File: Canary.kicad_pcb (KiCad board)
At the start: 4 copper layers, 56 x 38 mm, 85 parts, among them J1 CONN_ARM_CM_JTAG_SWD_10, J2 20021311-00010T4LF, J3 USB4125-GF-A, J4 S2B-PH-SM4-TB, Q1 PMN30UNX, Q2 PMN42XPEAH, Q3 PMN30UNX, SW1 TL3301SPF160QJ, U1 BMD-300-A-R, U10 LP5907MFX-3.2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

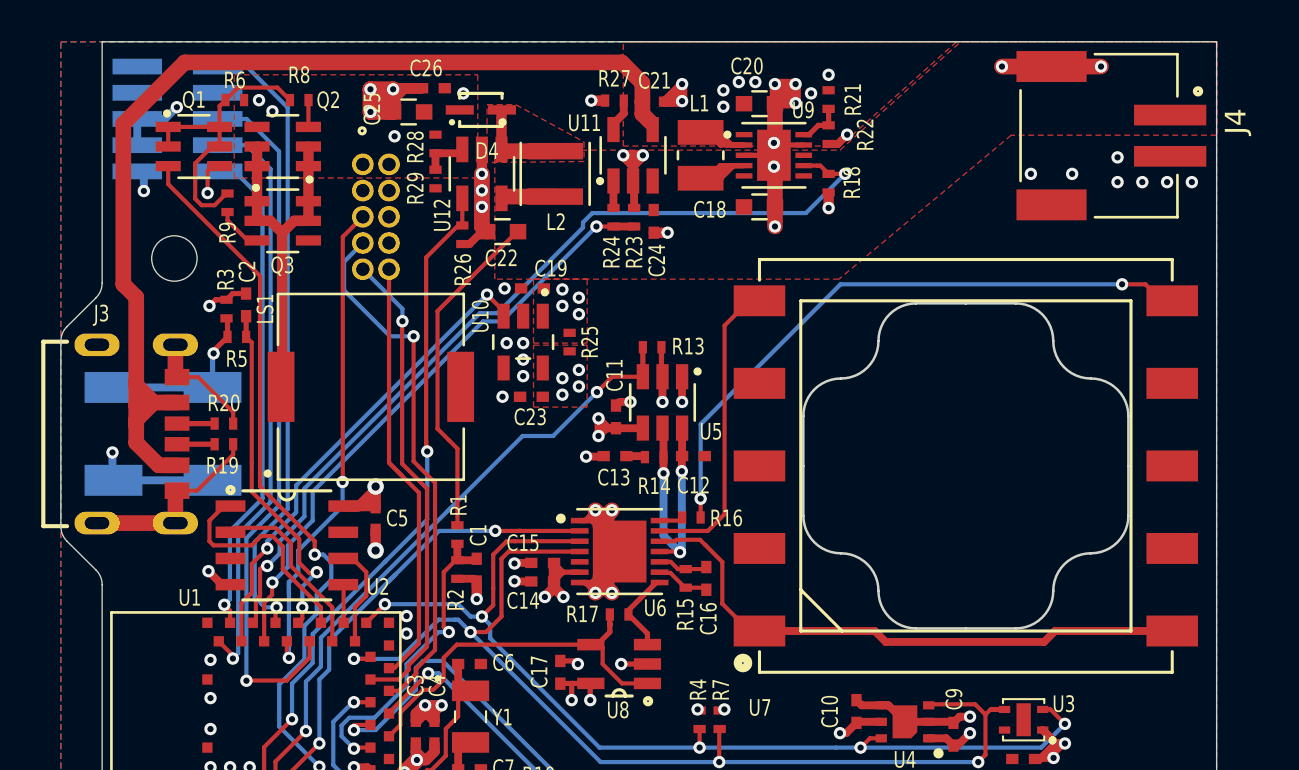
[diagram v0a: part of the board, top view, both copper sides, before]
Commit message: Change crystal
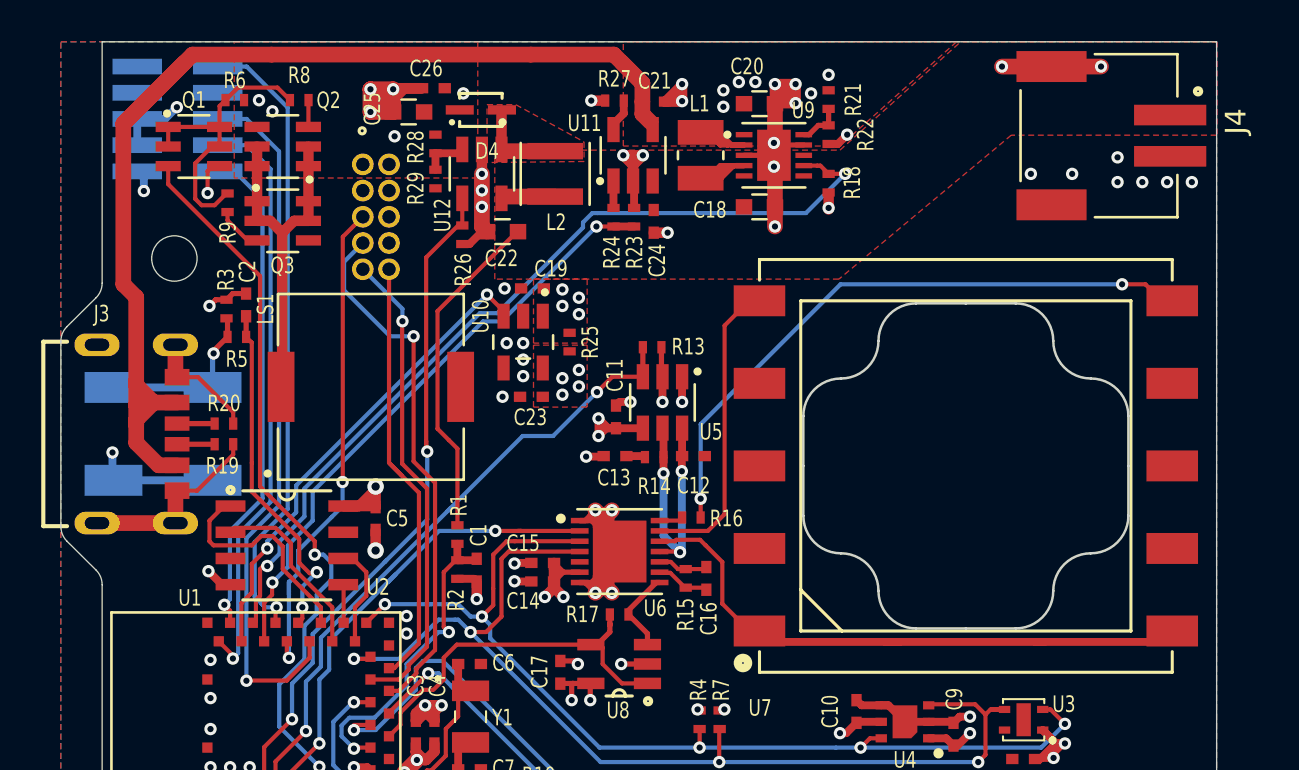
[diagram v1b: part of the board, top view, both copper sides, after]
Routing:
- net VBUS: track 51.8 -> 57.8 mm
- net /Potentiostat/SPEC_WE: track 28.0 -> 29.0 mm
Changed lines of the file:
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@@
     (thickness 1.6)
     (drawings 12)
-    (tracks 942)
+    (tracks 948)
     (zones 0)
     (modules 85)
@@
   )
   (setup
-    (last_trace_width 0.2032)
+    (last_trace_width 0.381)
     (user_trace_width 0.1524)
     (user_trace_width 0.2032)
@@
     (add_net ~RESET~)
   )
+  (module JetkovKiCADLib:SM-UART-04L locked (layer F.Cu)
+    (at 50.26 48.045)
+    (attr virtual)
+    (fp_text reference S1 (at 48.89 36.48) (layer F.SilkS) hide
+      (effects (font (size 0.8 0.6) (thickness 0.15)))
+    )
+    (fp_text value DNP (at 23.1 16.9) (layer F.Fab) hide
+      (effects (font (size 1 1) (thickness 0.15)))
+    )
+    (fp_line (start 7.65 11.47) (end 4.35 11.47) (layer Dwgs.User) (width 0.12))
+    (fp_line (start 4.35 4.53) (end 4.35 11.47) (layer Dwgs.User) (width 0.12))
+    (fp_line (start 9.5 13.5) (end 2.5 13.5) (layer Dwgs.User) (width 0.12))
+    (fp_line (start 7.65 11.47) (end 7.65 4.53) (layer Dwgs.User) (width 0.12))
+    (fp_line (start 9.5 2.5) (end 9.5 13.5) (layer Dwgs.User) (width 0.12))
+    (fp_line (start 2.5 2.5) (end 9.5 2.5) (layer Dwgs.User) (width 0.12))
+    (fp_line (start 4.35 4.53) (end 7.65 4.53) (layer Dwgs.User) (width 0.12))
+    (fp_line (start 2.5 13.5) (end 2.5 2.5) (layer Dwgs.User) (width 0.12))
+    (fp_line (start 0 0) (end 0 37) (layer Dwgs.User) (width 0.12))
+    (fp_line (start 0 37) (end 48 37) (layer Dwgs.User) (width 0.12))
+    (fp_line (start 48 37) (end 48 1) (layer Dwgs.User) (width 0.12))
+    (fp_line (start 48 1) (end 48 0) (layer Dwgs.User) (width 0.12))
+    (fp_line (start 48 0) (end 0 0) (layer Dwgs.User) (width 0.12))
+    (fp_text user 10 (at 8.4 12.5) (layer Dwgs.User)
+      (effects (font (size 0.8 0.8) (thickness 0.15)))
+    )
+    (fp_text user 9 (at 3.5 12.5) (layer Dwgs.User)
+      (effects (font (size 0.8 0.8) (thickness 0.15)))
+    )
+    (fp_text user 2 (at 8.6 3.6) (layer Dwgs.User)
+      (effects (font (size 0.8 0.8) (thickness 0.15)))
+    )
+    (fp_text user 1 (at 3.5 3.6) (layer Dwgs.User)
+      (effects (font (size 0.8 0.8) (thickness 0.15)))
+    )
+    (model :JetkovKiCADLib:SM-UART-04L.step
+      (offset (xyz 24 -18.5 -3))
+      (scale (xyz 1 1 1))
+      (rotate (xyz 180 0 0))
+    )
+  )
   (module JetkovKiCADLib:TL3301EF160QJ locked (layer B.Cu)
     (at 45.95 67)
@@
     )
   )
-  (module JetkovKiCADLib:SM-UART-04L locked (layer F.Cu)
-    (at 50.26 48.045)
-    (attr virtual)
-    (fp_text reference S1 (at 48.89 36.48) (layer F.SilkS) hide
-      (effects (font (size 0.8 0.6) (thickness 0.15)))
-    )
-    (fp_text value DNP (at 23.1 16.9) (layer F.Fab) hide
-      (effects (font (size 1 1) (thickness 0.15)))
-    )
-    (fp_line (start 7.65 11.47) (end 4.35 11.47) (layer Dwgs.User) (width 0.12))
-    (fp_line (start 4.35 4.53) (end 4.35 11.47) (layer Dwgs.User) (width 0.12))
-    (fp_line (start 9.5 13.5) (end 2.5 13.5) (layer Dwgs.User) (width 0.12))
-    (fp_line (start 7.65 11.47) (end 7.65 4.53) (layer Dwgs.User) (width 0.12))
-    (fp_line (start 9.5 2.5) (end 9.5 13.5) (layer Dwgs.User) (width 0.12))
-    (fp_line (start 2.5 2.5) (end 9.5 2.5) (layer Dwgs.User) (width 0.12))
-    (fp_line (start 4.35 4.53) (end 7.65 4.53) (layer Dwgs.User) (width 0.12))
-    (fp_line (start 2.5 13.5) (end 2.5 2.5) (layer Dwgs.User) (width 0.12))
-    (fp_line (start 0 0) (end 0 37) (layer Dwgs.User) (width 0.12))
-    (fp_line (start 0 37) (end 48 37) (layer Dwgs.User) (width 0.12))
-    (fp_line (start 48 37) (end 48 1) (layer Dwgs.User) (width 0.12))
-    (fp_line (start 48 1) (end 48 0) (layer Dwgs.User) (width 0.12))
-    (fp_line (start 48 0) (end 0 0) (layer Dwgs.User) (width 0.12))
-    (fp_text user 10 (at 8.4 12.5) (layer Dwgs.User)
-      (effects (font (size 0.8 0.8) (thickness 0.15)))
-    )
-    (fp_text user 9 (at 3.5 12.5) (layer Dwgs.User)
-      (effects (font (size 0.8 0.8) (thickness 0.15)))
-    )
-    (fp_text user 2 (at 8.6 3.6) (layer Dwgs.User)
-      (effects (font (size 0.8 0.8) (thickness 0.15)))
-    )
-    (fp_text user 1 (at 3.5 3.6) (layer Dwgs.User)
-      (effects (font (size 0.8 0.8) (thickness 0.15)))
-    )
-    (model :JetkovKiCADLib:SM-UART-04L.step
-      (offset (xyz 24 -18.5 -3))
-      (scale (xyz 1 1 1))
-      (rotate (xyz 180 0 0))
-    )
-  )
   (module Mounting_Holes:MountingHole_2.2mm_M2 locked (layer F.Cu)
     (at 46.5 58.5)
@@
   (segment (start 44.025 51.975) (end 44.025 59.75) (width 0.762) (layer F.Cu) (net 9))
   (segment (start 47 49) (end 44.025 51.975) (width 0.762) (layer F.Cu) (net 9))
-  (segment (start 68.175 49) (end 47 49) (width 0.762) (layer F.Cu) (net 9))
   (segment (start 69.175 50) (end 68.175 49) (width 0.762) (layer F.Cu) (net 9))
   (segment (start 69.175 50.9) (end 69.175 50) (width 0.762) (layer F.Cu) (net 9))
+  (segment (start 47.38 48.62) (end 51.21 48.62) (width 0.762) (layer F.Cu) (net 9))
+  (segment (start 44.025 51.975) (end 47.38 48.62) (width 0.762) (layer F.Cu) (net 9))
+  (segment (start 67.795 48.62) (end 69.175 50) (width 0.762) (layer F.Cu) (net 9))
+  (segment (start 63.77 48.62) (end 67.795 48.62) (width 0.762) (layer F.Cu) (net 9))
+  (segment (start 63.77 48.62) (end 51.21 48.62) (width 0.762) (layer F.Cu) (net 9))
   (via (at 50.6 50.83) (size 0.6) (drill 0.3) (layers F.Cu B.Cu) (net 10))
   (via (at 51.25 51.37) (size 0.6) (drill 0.3) (layers F.Cu B.Cu) (net 10))
@@
   (segment (start 70.98 71.2) (end 70.01 71.2) (width 0.2032) (layer F.Cu) (net 53))
   (segment (start 71.1 71.08) (end 70.98 71.2) (width 0.2032) (layer F.Cu) (net 53))
-  (segment (start 94.85 76.55) (end 89.17 76.55) (width 0.381) (layer F.Cu) (net 54))
-  (segment (start 89.17 76.55) (end 88.64 77.08) (width 0.381) (layer F.Cu) (net 54))
-  (segment (start 88.64 77.08) (end 80.97 77.08) (width 0.381) (layer F.Cu) (net 54))
-  (segment (start 80.44 76.55) (end 74.85 76.55) (width 0.381) (layer F.Cu) (net 54))
-  (segment (start 80.97 77.08) (end 80.44 76.55) (width 0.381) (layer F.Cu) (net 54))
   (segment (start 73.05 75.23) (end 74.45 76.63) (width 0.2032) (layer F.Cu) (net 54))
   (segment (start 73.05 73.207202) (end 73.05 75.23) (width 0.2032) (layer F.Cu) (net 54))
@@
   (segment (start 72.237202 72.397202) (end 71.97 72.13) (width 0.2032) (layer F.Cu) (net 54))
   (segment (start 72.24 72.397202) (end 72.237202 72.397202) (width 0.2032) (layer F.Cu) (net 54))
+  (segment (start 75.38 77.08) (end 81.62 77.08) (width 0.381) (layer F.Cu) (net 54))
+  (segment (start 74.85 76.55) (end 75.38 77.08) (width 0.381) (layer F.Cu) (net 54))
+  (segment (start 81.62 77.08) (end 80.97 77.08) (width 0.381) (layer F.Cu) (net 54))
+  (segment (start 94.32 77.08) (end 88.22 77.08) (width 0.381) (layer F.Cu) (net 54))
+  (segment (start 94.85 76.55) (end 94.32 77.08) (width 0.381) (layer F.Cu) (net 54))
+  (segment (start 88.22 77.08) (end 81.62 77.08) (width 0.381) (layer F.Cu) (net 54))
+  (segment (start 88.64 77.08) (end 88.22 77.08) (width 0.381) (layer F.Cu) (net 54))
   (segment (start 73.16 61.75) (end 74.44 60.47) (width 0.2032) (layer F.Cu) (net 55))
   (segment (start 73.16 70.89) (end 73.16 61.75) (width 0.2032) (layer F.Cu) (net 55))
@@
     (polygon
       (pts
-        (xy 61.2 54.6) (xy 49.4 54.6) (xy 49.4 49.6) (xy 61.2 49.6)
+        (xy 61.2 54.6) (xy 49.4 54.6) (xy 49.4 48) (xy 61.2 48)
       )
     )
@@
     (polygon
       (pts
-        (xy 68 62.6) (xy 62.1 62.6) (xy 62.1 86) (xy 41 86.05) (xy 41 48.05)
+        (xy 68 62.6) (xy 62.1 62.6) (xy 62.1 86) (xy 41 86) (xy 41 48)
         (xy 84.4 48.05)
       )
@@
       )
     )
+  )
+  (zone (net 0) (net_name "") (layers F.Cu GND.Cu PWR.Cu B.Cu) (hatch edge 0.508)
+    (connect_pads (clearance 0.2032))
+    (min_thickness 0.254)
+    (keepout (tracks not_allowed) (vias not_allowed) (copperpour not_allowed))
+    (fill (arc_segments 32) (thermal_gap 0.508) (thermal_bridge_width 0.508))
+    (polygon
+      (pts
+        (xy 92.8 61.9) (xy 92.8 75.2) (xy 91.5 76.5) (xy 78.2 76.5) (xy 76.9 75.2)
+        (xy 76.9 61.9) (xy 78.2 60.6) (xy 91.5 60.6)
+      )
+    )

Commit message: Change crystal again
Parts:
- Y1: footprint JetkovKiCADLib:FC135327680KAAC3 -> JetkovKiCADLib:ECS-327-9-12-C-TR
- moved C6 1.60 mm to (60.9, 79.8)
- moved Y1 0.81 mm to (60.8, 81.5)
- moved C7 0.05 mm to (60.9, 83.2)
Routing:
- net I2C_SCL: track 49.2 -> 54.0 mm
- net /XTAL2: track 11.8 -> 9.76 mm
- net I2C_SDA: track 51.9 -> 52.7 mm
- net LMP_VOUT_B: track 19.0 -> 18.4 mm

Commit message: Add canary logo
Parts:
- added H2: MountingHole, Mounting_Holes:MountingHole_2.2mm_M2, F.Cu at (94.5, 83.5)
- added LOGO1: CANARY-LOGO, JetkovKiCADLib:CANARY-LOGO, B.Cu at (86.2, 55.9)
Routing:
- net GND: vias 69 -> 74
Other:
- board text added: "Alex Petkovic"
- board text added: "PROJECT CANARY"
- board text added: "Rev A.1"

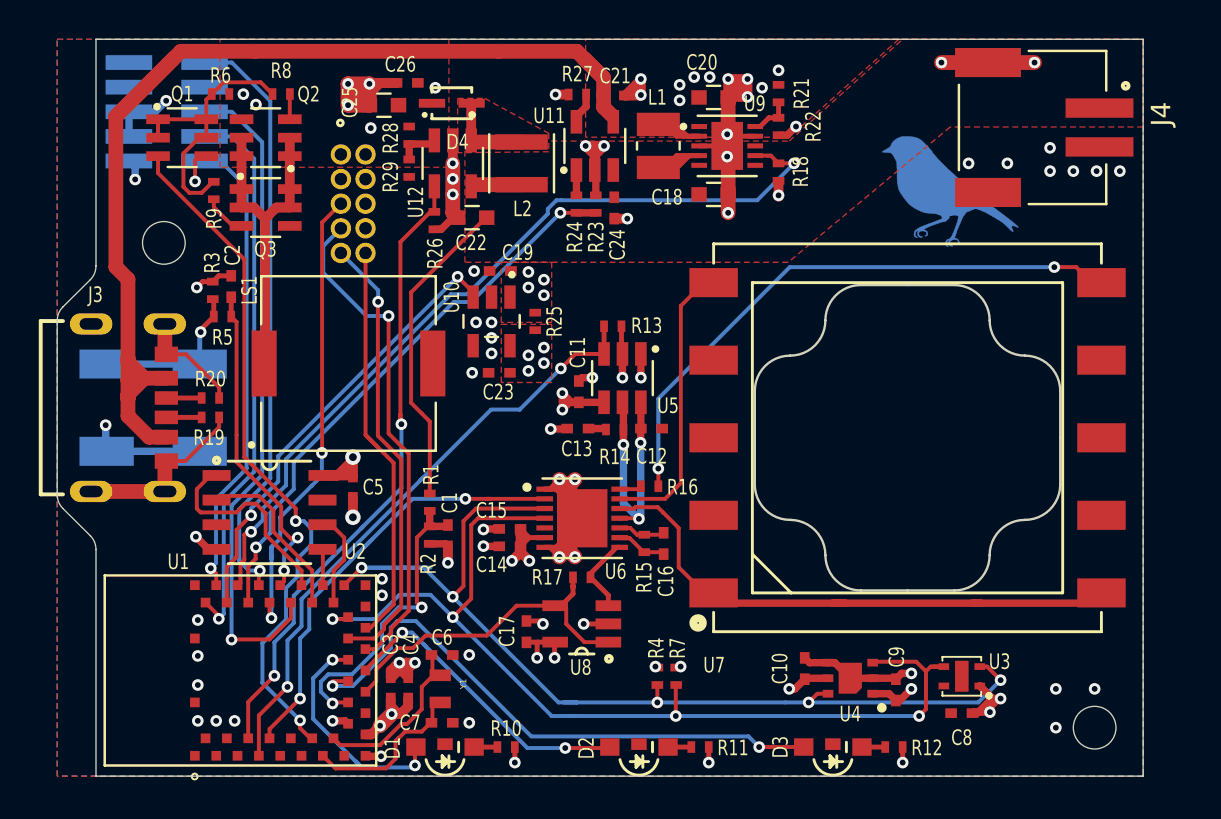
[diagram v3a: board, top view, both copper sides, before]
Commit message: Add TVS diodes, piezo resistor, testpoint, cleanup
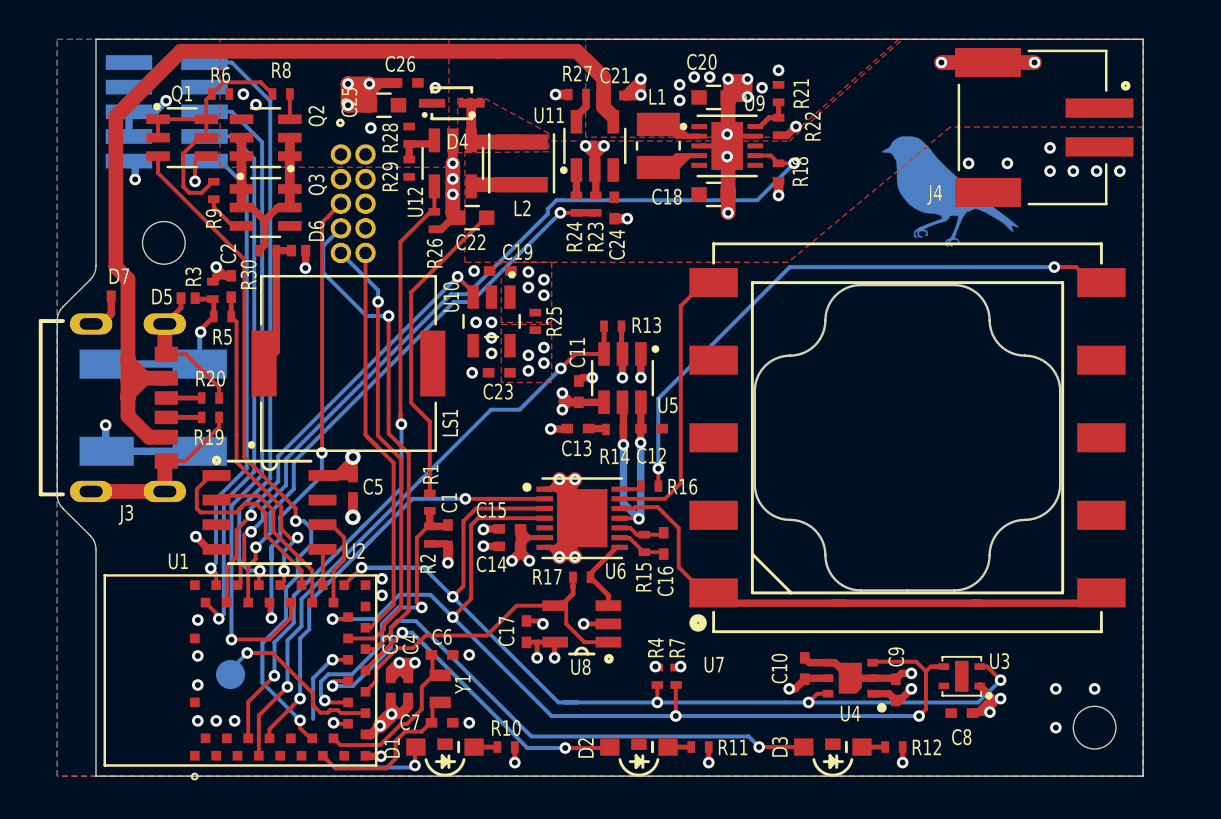
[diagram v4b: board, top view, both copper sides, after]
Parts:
- added D5: D_Schottky_ALT, JetkovKiCADLib:NSPU3051, F.Cu at (47.8, 61.4)
- added D6: D_Schottky_ALT, JetkovKiCADLib:NSPU3051, F.Cu at (53.5, 58.9)
- added D7: D_Schottky_ALT, JetkovKiCADLib:NSPU3051, F.Cu at (44.1, 61.2)
- added R30: 487k, JetkovKiCADLib:R_0402_NoSilk, F.Cu at (51.9, 58.9)
- added TP1: TestPoint, Measurement_Points:Measurement_Point_Round-SMD-Pad_Small, B.Cu at (49.9, 80.8)
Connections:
- Q2 pad 1: /PDRIVE_O -> Net-(Q2-Pad1)
- Q2 pad 2: /PDRIVE_O -> Net-(Q2-Pad1)
- Q2 pad 5: /PDRIVE_O -> Net-(Q2-Pad1)
- Q2 pad 6: /PDRIVE_O -> Net-(Q2-Pad1)
- Q3 pad 1: /PDRIVE_O -> Net-(Q2-Pad1)
- Q3 pad 2: /PDRIVE_O -> Net-(Q2-Pad1)
- Q3 pad 5: /PDRIVE_O -> Net-(Q2-Pad1)
- Q3 pad 6: /PDRIVE_O -> Net-(Q2-Pad1)
- U1 pad 19: (no net) -> Net-(TP1-Pad1)
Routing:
- net Net-(Q2-Pad1): track 0.00 -> 11.9 mm
- net /PDRIVE_O: track 17.7 -> 8.26 mm
- net Net-(TP1-Pad1): track 0.00 -> 9.31 mm, vias 0 -> 1
- net GND: track 117.4 -> 122.9 mm, vias 74 -> 75
- net LED_GREEN: track 11.8 -> 8.06 mm
- net /RBTN: track 8.47 -> 9.40 mm
